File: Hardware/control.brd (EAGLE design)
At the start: 100 x 80 mm, 11 parts, among them IC1 317T

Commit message: Added some better schematics
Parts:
- removed C1: 100uF, Rodentometer:C050-024X044
- removed C2: 100uF, Rodentometer:C075-032X103
- removed JP1: (no value), Rodentometer:1X06
- removed JP2: (no value), Rodentometer:1X02
- removed JP3: (no value), Rodentometer:1X04
- added ARDUINO_DATA, ARDUINO_POWER: (no value), Rodentometer:1X06
- added LCD: (no value), Rodentometer:1X04
- added POWER, RESET_SWITCH: (no value), Rodentometer:1X02
- added R6: 10k, Rodentometer:0207/7
- added SENSOR, SWITCHES: (no value), Rodentometer:1X03
- R3: device Rodentometer:0204/7 -> Rodentometer:0207/10
- moved IC1 51.6 mm to (53.3, 17.8), turned to 270 degrees
- moved R1 23.2 mm to (34.3, 35.6)
- moved R4 20.8 mm to (58.4, 31.8), turned to 90 degrees
- moved R2 20.7 mm to (47.0, 35.6)
- moved R3 18.3 mm to (55.9, 30.5), turned to 90 degrees
- moved R5 17.8 mm to (47.0, 33.0), turned to 0 degrees
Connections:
- removed net N$1: IC1.2, JP1.1, R1.1
- removed net N$2: IC1.3, JP2.2
- removed net N$3: C2.1, JP3.1, R3.2
- removed net N$4: C1.1, JP3.2, R4.2
- removed net N$6: JP1.6, JP3.3, R5.1
- new net HALL: ARDUINO_DATA.5, R6.1, SENSOR.3
- new net LCD_RX: ARDUINO_DATA.4, LCD.4
- new net LCD_TX: ARDUINO_DATA.3, LCD.3
- new net RESET: ARDUINO_POWER.6, R5.1, RESET_SWITCH.1
- new net SW_A: ARDUINO_DATA.1, R3.1, SWITCHES.1
- new net SW_B: ARDUINO_DATA.2, R4.1, SWITCHES.2
- new net VCC: IC1.3, POWER.2
- new net VIN: ARDUINO_POWER.1, IC1.2, LCD.1, R1.1
- net +5V: now also ARDUINO_POWER.4, SENSOR.1, SWITCHES.3; no longer JP1.4, R3.1, R4.1
- net GND: now also ARDUINO_POWER.2, ARDUINO_POWER.3, LCD.2, POWER.1, R3.2, R4.2, R6.2, RESET_SWITCH.2, SENSOR.2; no longer C1.2, C2.2, JP1.2, JP1.3, JP2.1, JP3.4
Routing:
- net RESET: track 0.00 -> 88.9 mm, vias 0 -> 8
- net VIN: track 0.00 -> 81.3 mm, vias 0 -> 2
- net +5V: track 53.3 -> 129.5 mm, vias 4 -> 8
- net SW_B: track 0.00 -> 73.7 mm, vias 0 -> 2
- net HALL: track 0.00 -> 71.1 mm, vias 0 -> 4
- net N$6: track 71.1 -> 0.00 mm, vias 2 -> 0
- net SW_A: track 0.00 -> 68.6 mm, vias 0 -> 2
- net LCD_TX: track 0.00 -> 61.0 mm
- net LCD_RX: track 0.00 -> 61.0 mm
- net VCC: track 0.00 -> 50.8 mm, vias 0 -> 2
- net N$2: track 33.0 -> 0.00 mm, vias 2 -> 0
- net N$1: track 30.5 -> 0.00 mm, vias 2 -> 0
- net GND: track 101.6 -> 127.0 mm, vias 5 -> 11
- net N$4: track 12.7 -> 0.00 mm
- net N$3: track 12.7 -> 0.00 mm
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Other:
- board size 100 x 80 mm -> 94.9 x 40.6 mm
- board text added: "+3.3V"
- board text added: "+5V"
- board text added: "GND"
- board text added: "HALL"
- board text added: "LCD_RX"
- board text added: "LCD_TX"
- board text added: "Reset"
- board text added: "SW_A"
- board text added: "SW_B"
- board text added: "Vcc"
- board text added: "Vin"

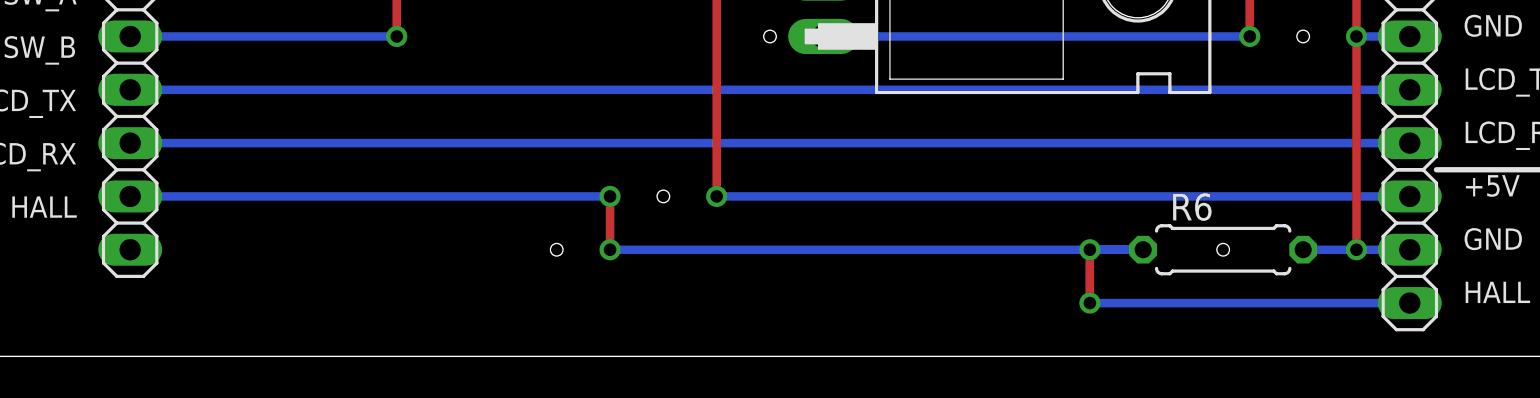
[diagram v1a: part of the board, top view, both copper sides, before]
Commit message: Fixed error in schematics and updated code to use Interrupt
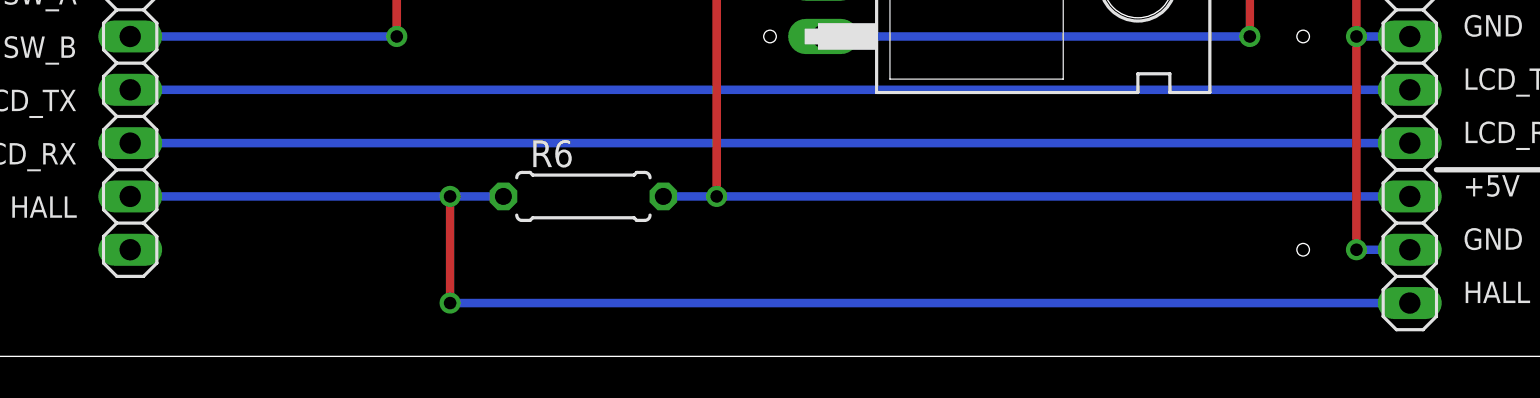
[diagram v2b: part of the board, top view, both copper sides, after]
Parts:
- moved R6 30.6 mm to (31.8, 7.62)
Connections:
- net +5V: now also R6.2
- net GND: no longer R6.2
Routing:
- net HALL: track 71.1 -> 68.6 mm, vias 4 -> 2
- net GND: track 127.0 -> 124.5 mm
- net +5V: track 129.5 -> 132.1 mm
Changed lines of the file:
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@@
 <hole x="46.99" y="35.56" drill="0.6"/>
 <hole x="46.99" y="33.02" drill="0.6"/>
-<hole x="35.56" y="7.62" drill="0.6"/>
-<hole x="30.48" y="5.08" drill="0.6"/>
-<hole x="62.23" y="5.08" drill="0.6"/>
 <wire x1="72.39" y1="8.89" x2="92.71" y2="8.89" width="0.254" layer="25"/>
 <wire x1="72.39" y1="19.05" x2="92.71" y2="19.05" width="0.254" layer="25"/>
@@
 <text x="7.62" y="10.16" size="1.016" layer="25" rot="R180">LCD_RX</text>
 <text x="7.62" y="7.62" size="1.016" layer="25" rot="R180">HALL</text>
+<hole x="66.04" y="5.08" drill="0.6"/>
 </plain>
 <attributes>
@@
 <attribute name="VALUE" x="67.945" y="8.89" size="1.27" layer="27" rot="R270"/>
 </element>
-<element name="R6" library="Rodentometer" package="0207/7" value="10k" x="62.23" y="5.08" smashed="yes">
-<attribute name="NAME" x="59.69" y="6.477" size="1.27" layer="25" ratio="10"/>
-<attribute name="VALUE" x="59.309" y="4.5212" size="1.27" layer="27" ratio="10"/>
+<element name="R6" library="Rodentometer" package="0207/7" value="10k" x="31.75" y="7.62" smashed="yes">
+<attribute name="NAME" x="29.21" y="9.017" size="1.27" layer="25" ratio="10"/>
+<attribute name="VALUE" x="28.829" y="7.0612" size="1.27" layer="27" ratio="10"/>
 </element>
 </elements>
@@
 <wire x1="68.58" y1="15.24" x2="71.12" y2="15.24" width="0.4064" layer="16"/>
 <contactref element="SENSOR" pad="2"/>
-<contactref element="R6" pad="2"/>
-<wire x1="68.58" y1="5.08" x2="66.04" y2="5.08" width="0.4064" layer="16"/>
 <wire x1="71.12" y1="5.08" x2="68.58" y2="5.08" width="0.4064" layer="16"/>
 <via x="68.58" y="5.08" extent="1-16" drill="0.6" shape="square"/>
@@
 <via x="68.58" y="33.02" extent="1-16" drill="0.6" shape="square"/>
 <wire x1="68.58" y1="33.02" x2="53.34" y2="33.02" width="0.4064" layer="16"/>
+<contactref element="R6" pad="2"/>
+<wire x1="35.56" y1="7.62" x2="38.1" y2="7.62" width="0.4064" layer="16"/>
 </signal>
 <signal name="RESET">
@@
 <contactref element="ARDUINO_DATA" pad="5"/>
 <contactref element="R6" pad="1"/>
-<wire x1="71.12" y1="2.54" x2="55.88" y2="2.54" width="0.4064" layer="16"/>
-<via x="55.88" y="2.54" extent="1-16" drill="0.6" shape="square"/>
-<wire x1="55.88" y1="2.54" x2="55.88" y2="5.08" width="0.4064" layer="1"/>
-<via x="55.88" y="5.08" extent="1-16" drill="0.6" shape="square"/>
-<wire x1="55.88" y1="5.08" x2="58.42" y2="5.08" width="0.4064" layer="16"/>
-<wire x1="58.42" y1="5.08" x2="33.02" y2="5.08" width="0.4064" layer="16"/>
-<via x="33.02" y="5.08" extent="1-16" drill="0.6" shape="square"/>
-<wire x1="33.02" y1="5.08" x2="33.02" y2="7.62" width="0.4064" layer="1"/>
-<via x="33.02" y="7.62" extent="1-16" drill="0.6" shape="square"/>
-<wire x1="33.02" y1="7.62" x2="10.16" y2="7.62" width="0.4064" layer="16"/>
+<wire x1="71.12" y1="2.54" x2="25.4" y2="2.54" width="0.4064" layer="16"/>
+<via x="25.4" y="2.54" extent="1-16" drill="0.6" shape="square"/>
+<wire x1="25.4" y1="2.54" x2="25.4" y2="7.62" width="0.4064" layer="1"/>
+<via x="25.4" y="7.62" extent="1-16" drill="0.6" shape="square"/>
+<wire x1="25.4" y1="7.62" x2="10.16" y2="7.62" width="0.4064" layer="16"/>
+<wire x1="27.94" y1="7.62" x2="25.4" y2="7.62" width="0.4064" layer="16"/>
 </signal>
 </signals>

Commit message: Added some screenshots ready for blogging
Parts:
- R1: value 220 -> 220R
- R5: value (none) -> 100R
- moved IC1 7.62 mm to (45.7, 17.8)
- moved LCD 7.62 mm to (63.5, 14.0)
- moved POWER 7.62 mm to (63.5, 36.8)
- moved R2 7.62 mm to (39.4, 35.6)
- moved R3 7.62 mm to (48.3, 30.5)
- moved R4 7.62 mm to (50.8, 31.8)
- moved R5 7.62 mm to (39.4, 33.0)
- moved RESET_SWITCH 7.62 mm to (63.5, 21.6)
- moved SENSOR 7.62 mm to (63.5, 5.08)
- moved SWITCHES 7.62 mm to (63.5, 27.9)
- moved R6 7.62 mm to (24.1, 7.62)
- moved R1 7.62 mm to (26.7, 35.6)
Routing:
- net +5V: track 132.1 -> 124.5 mm
- net HALL: track 68.6 -> 61.0 mm
- net VIN: track 81.3 -> 73.7 mm
- net SW_B: track 73.7 -> 66.0 mm
- net SW_A: track 68.6 -> 61.0 mm
- net RESET: track 88.9 -> 81.3 mm
- net LCD_TX: track 61.0 -> 53.3 mm
- net LCD_RX: track 61.0 -> 53.3 mm
- net GND: track 124.5 -> 129.5 mm
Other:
- board size 94.9 x 40.6 mm -> 87.3 x 40.6 mm
